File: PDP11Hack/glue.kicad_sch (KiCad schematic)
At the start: 5 parts, among them U21 74HCT139, U22 74AHCT273, U23 74LS27, U24 74HCT04, U25 74LS153

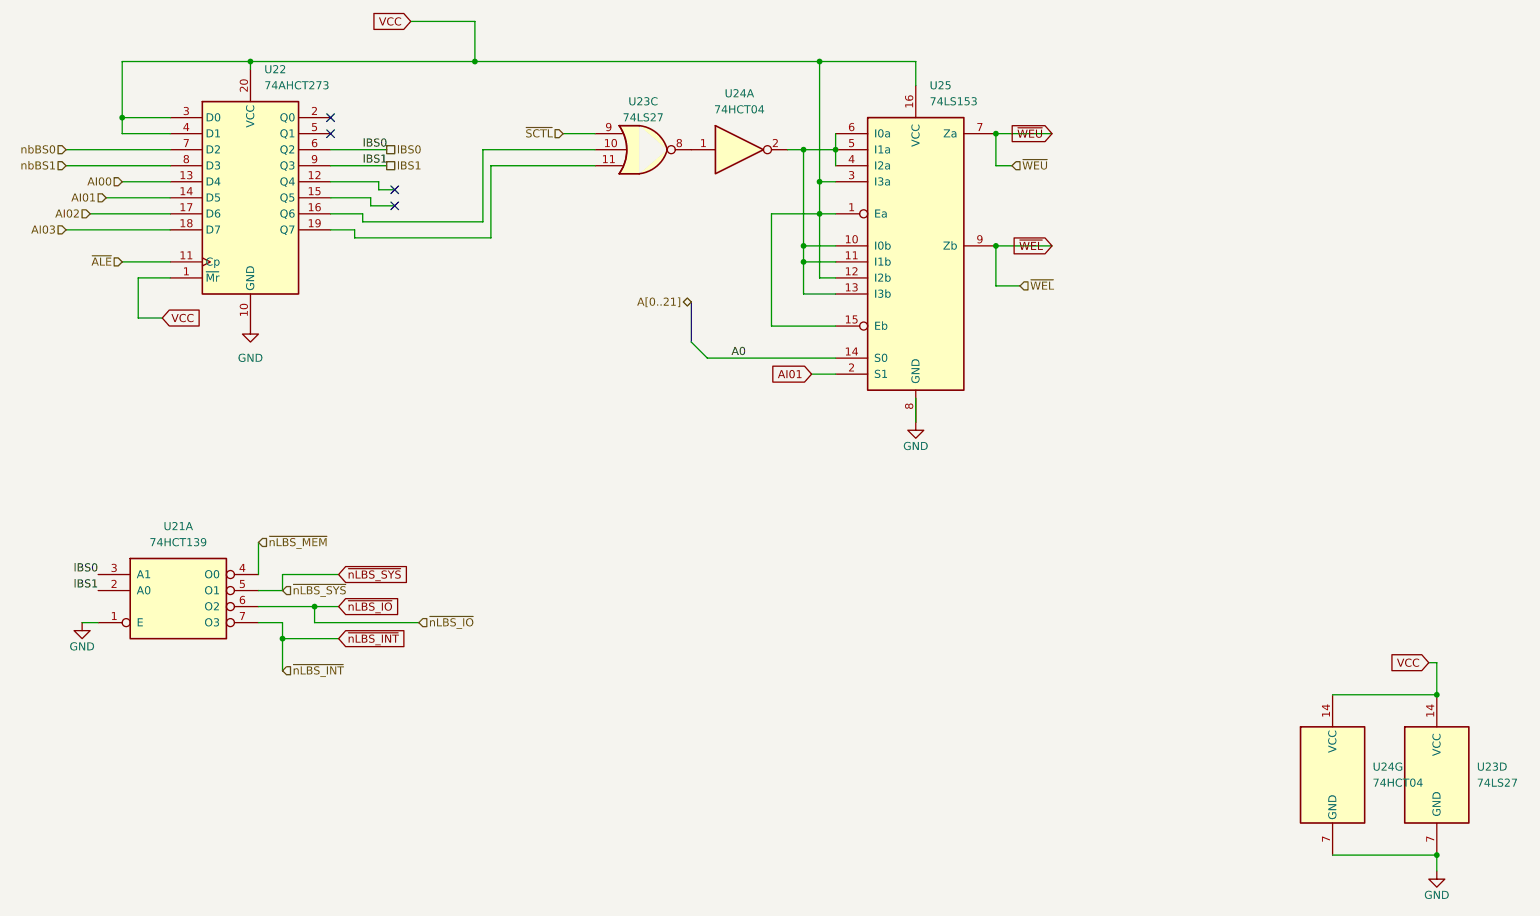
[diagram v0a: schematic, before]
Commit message: Corrections thanks to Peter Schranz on VCFED
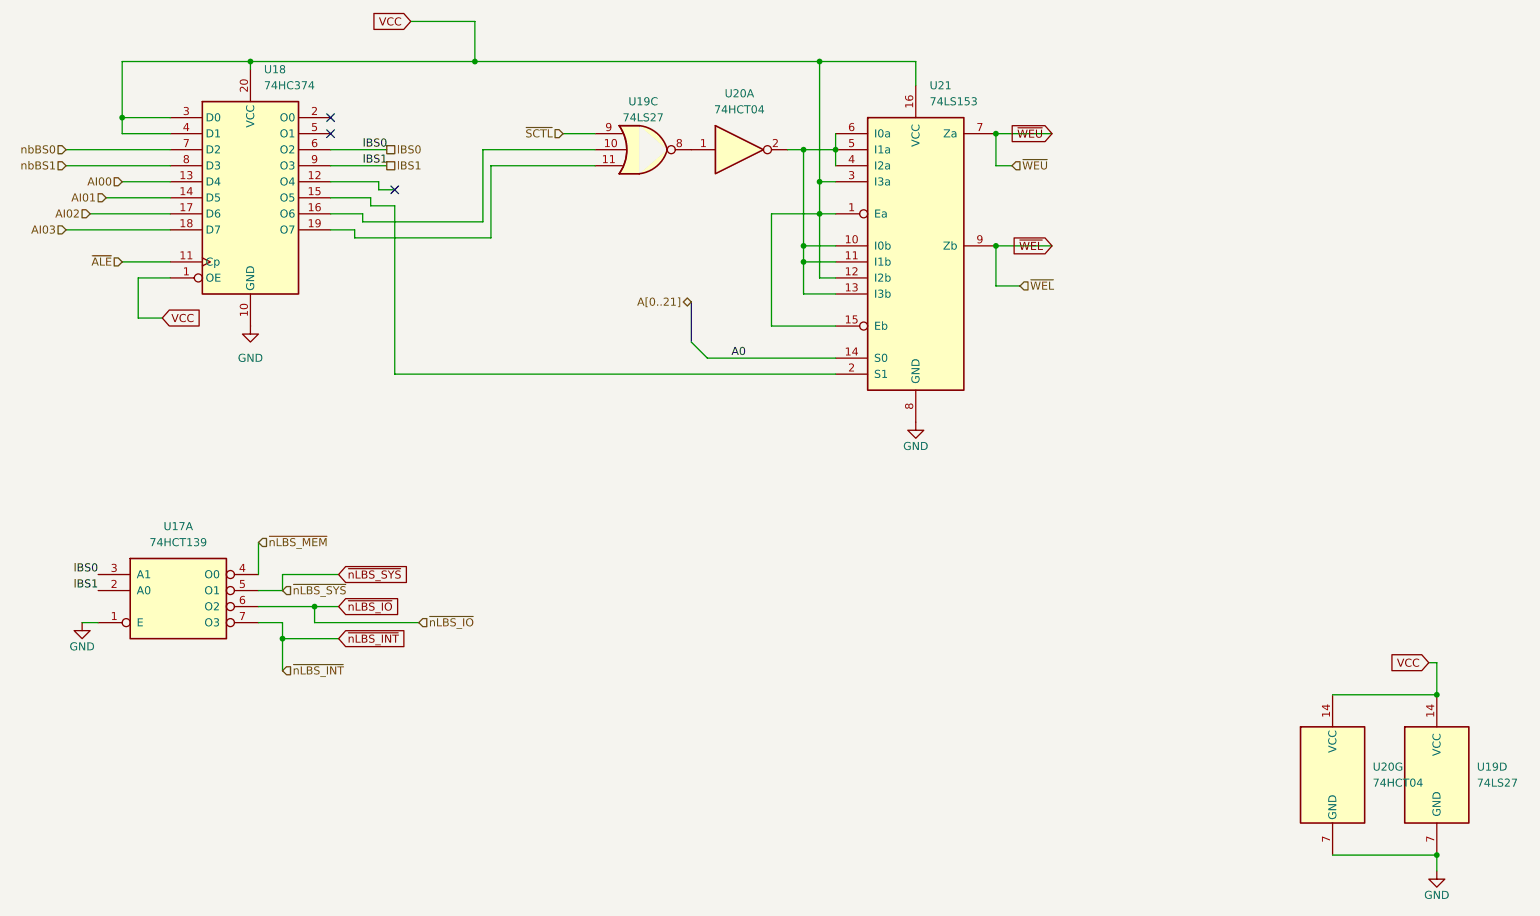
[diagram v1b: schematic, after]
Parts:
- removed U22: 74AHCT273, symbol 74xx:74AHCT273
- added U18: 74HC374, symbol 74xx:74HC374
- renumbered U21 to U17, U23 to U19, U24 to U20, U25 to U21
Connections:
- net AI00: now also U18.13 (D4)
- net AI01: now also U18.14 (D5); no longer U21.2 (S1)
- net AI02: now also U18.17 (D6)
- net AI03: now also U18.18 (D7)
- net GND: now also U18.10 (GND)
- net VCC: now also U18.1 (OE), U18.20 (VCC), U18.3 (D0), U18.4 (D1)
- net lBS0: now also U18.6 (O2)
- net lBS1: now also U18.9 (O3)
- net nbBS0: now also U18.7 (D2)
- net nbBS1: now also U18.8 (D3)
- net ~{ALE}: now also U18.11 (Cp)
- net at U19.10: now also U18.16 (O6)
- net at U19.11: now also U18.19 (O7)
- new net: U18.15 (O5), U21.2 (S1)
- no-connect marks 4 -> 3
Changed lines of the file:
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@@
-	)
-	(no_connect
-		(at 100.33 53.34)
 	)
 	(no_connect
@@
 	(wire
 		(pts
+			(xy 100.33 53.34) (xy 100.33 80.01)
+		)
+		(stroke
+			(width 0)
+			(type default)
+		)
+	)
+	(wire
+		(pts
 			(xy 78.74 116.84) (xy 87.63 116.84)
 		)
@@
 	(wire
 		(pts
-			(xy 166.37 80.01) (xy 170.18 80.01)
-		)
-		(stroke
-			(width 0)
-			(type default)
-		)
-	)
-	(wire
-		(pts
 			(xy 82.55 111.76) (xy 91.44 111.76)
 		)
@@
 	(wire
 		(pts
+			(xy 100.33 80.01) (xy 170.18 80.01)
+		)
+		(stroke
+			(width 0)
+			(type default)
+		)
+	)
+	(wire
+		(pts
 			(xy 90.17 54.61) (xy 95.25 54.61)
 		)
@@
 		(pts
 			(xy 57.15 49.53) (xy 64.77 49.53)
-		)
-		(stroke
-			(width 0)
-			(type default)
-		)
-	)
-	(wire
-		(pts
-			(xy 182.88 83.82) (xy 182.88 87.63)
 		)
 		(stroke
@@
 			)
 			(justify left bottom)
-		)
-	)
-	(global_label "AI01"
-		(shape input)
-		(at 166.37 80.01 180)
-		(fields_autoplaced yes)
-		(effects
-			(font
-				(size 1.27 1.27)
-			)
-			(justify right)
-		)
-		(property "Intersheetrefs" "${INTERSHEET_REFS}"
-			(at 159.2724 80.01 0)
-			(effects
-				(font
-					(size 1.27 1.27)
-				)
-				(justify right)
-				(hide yes)
-			)
 		)
 	)
@@
 		(dnp no)
 		(fields_autoplaced yes)
-		(property "Reference" "U23"
+		(property "Reference" "U19"
 			(at 139.7 36.83 0)
 			(effects
@@
 			(project "Modular DCJ11"
 				(path "/264d9b66-53d1-4564-94e8-42c7c0bb6a66/227e0659-a0cd-47a6-aec8-ce37362b6db6"
-					(reference "U23")
+					(reference "U19")
 					(unit 3)
 				)
@@
 		(dnp no)
 		(fields_autoplaced yes)
-		(property "Reference" "U25"
+		(property "Reference" "U21"
 			(at 185.0741 34.29 0)
 			(effects
@@
 			(project "Modular DCJ11"
 				(path "/264d9b66-53d1-4564-94e8-42c7c0bb6a66/227e0659-a0cd-47a6-aec8-ce37362b6db6"
-					(reference "U25")
+					(reference "U21")
 					(unit 1)
 				)
@@
 		(dnp no)
 		(fields_autoplaced yes)
-		(property "Reference" "U24"
+		(property "Reference" "U20"
 			(at 154.94 35.56 0)
 			(effects
@@
 			(project "Modular DCJ11"
 				(path "/264d9b66-53d1-4564-94e8-42c7c0bb6a66/227e0659-a0cd-47a6-aec8-ce37362b6db6"
-					(reference "U24")
+					(reference "U20")
 					(unit 1)
 				)
@@
 		(on_board yes)
 		(dnp no)
-		(property "Reference" "#PWR063"
+		(property "Reference" "#PWR061"
 			(at 182.88 93.98 0)
 			(effects
@@
 			(project "Modular DCJ11"
 				(path "/264d9b66-53d1-4564-94e8-42c7c0bb6a66/227e0659-a0cd-47a6-aec8-ce37362b6db6"
-					(reference "#PWR063")
+					(reference "#PWR061")
 					(unit 1)
 				)
@@
 		(on_board yes)
 		(dnp no)
-		(property "Reference" "#PWR061"
+		(property "Reference" "#PWR059"
 			(at 50.8 125.73 0)
 			(effects
@@
 			(project "Modular DCJ11"
 				(path "/264d9b66-53d1-4564-94e8-42c7c0bb6a66/227e0659-a0cd-47a6-aec8-ce37362b6db6"
-					(reference "#PWR061")
+					(reference "#PWR059")
 					(unit 1)
 				)
@@
 		(dnp no)
 		(fields_autoplaced yes)
-		(property "Reference" "U24"
+		(property "Reference" "U20"
 			(at 255.27 142.2399 0)
 			(effects
@@
 			(project "Modular DCJ11"
 				(path "/264d9b66-53d1-4564-94e8-42c7c0bb6a66/227e0659-a0cd-47a6-aec8-ce37362b6db6"
-					(reference "U24")
+					(reference "U20")
 					(unit 7)
+				)
+			)
+		)
+	)
+	(symbol
+		(lib_id "74xx:74HC374")
+		(at 77.47 52.07 0)
+		(unit 1)
+		(exclude_from_sim no)
+		(in_bom yes)
+		(on_board yes)
+		(dnp no)
+		(fields_autoplaced yes)
+		(property "Reference" "U18"
+			(at 79.6133 31.75 0)
+			(effects
+				(font
+					(size 1.27 1.27)
+				)
+				(justify left)
+			)
+		)
+		(property "Value" "74HC374"
+			(at 79.6133 34.29 0)
+			(effects
+				(font
+					(size 1.27 1.27)
+				)
+				(justify left)
+			)
+		)
+		(property "Footprint" ""
+			(at 77.47 52.07 0)
+			(effects
+				(font
+					(size 1.27 1.27)
+				)
+				(hide yes)
+			)
+		)
+		(property "Datasheet" "https://www.ti.com/lit/ds/symlink/cd74hct374.pdf"
+			(at 77.47 52.07 0)
+			(effects
+				(font
+					(size 1.27 1.27)
+				)
+				(hide yes)
+			)
+		)
+		(property "Description" "8-bit Register, 3-state outputs"
+			(at 77.47 52.07 0)
+			(effects
+				(font
+					(size 1.27 1.27)
+				)
+				(hide yes)
+			)
+		)
+		(pin "10"
+		)
+		(pin "14"
+		)
+		(pin "17"
+		)
+		(pin "11"
+		)
+		(pin "16"
+		)
+		(pin "15"
+		)
+		(pin "1"
+		)
+		(pin "7"
+		)
+		(pin "4"
+		)
+		(pin "18"
+		)
+		(pin "3"
+		)
+		(pin "5"
+		)
+		(pin "20"
+		)
+		(pin "6"
+		)
+		(pin "2"
+		)
+		(pin "19"
+		)
+		(pin "12"
+		)
+		(pin "9"
+		)
+		(pin "8"
+		)
+		(pin "13"
+		)
+		(instances
+			(project ""
+				(path "/264d9b66-53d1-4564-94e8-42c7c0bb6a66/227e0659-a0cd-47a6-aec8-ce37362b6db6"
+					(reference "U18")
+					(unit 1)
 				)
 			)
@@
 		(on_board yes)
 		(dnp no)
-		(property "Reference" "#PWR074"
+		(property "Reference" "#PWR062"
 			(at 265.43 165.1 0)
 			(effects
@@
 			(project "Modular DCJ11"
 				(path "/264d9b66-53d1-4564-94e8-42c7c0bb6a66/227e0659-a0cd-47a6-aec8-ce37362b6db6"
-					(reference "#PWR074")
+					(reference "#PWR062")
 					(unit 1)
 				)
@@
 		(dnp no)
 		(fields_autoplaced yes)
-		(property "Reference" "U23"
+		(property "Reference" "U19"
 			(at 271.78 142.2399 0)
 			(effects
@@
 			(project "Modular DCJ11"
 				(path "/264d9b66-53d1-4564-94e8-42c7c0bb6a66/227e0659-a0cd-47a6-aec8-ce37362b6db6"
-					(reference "U23")
+					(reference "U19")
 					(unit 4)
 				)
@@
 		(dnp no)
 		(fields_autoplaced yes)
-		(property "Reference" "U21"
+		(property "Reference" "U17"
 			(at 66.04 104.14 0)
 			(effects
@@
 			(project "Modular DCJ11"
 				(path "/264d9b66-53d1-4564-94e8-42c7c0bb6a66/227e0659-a0cd-47a6-aec8-ce37362b6db6"
-					(reference "U21")
+					(reference "U17")
 					(unit 1)
 				)
@@
 		(dnp no)
 		(fields_autoplaced yes)
-		(property "Reference" "#PWR062"
+		(property "Reference" "#PWR060"
 			(at 77.47 78.74 0)
 			(effects
@@
 			(project "Modular DCJ11"
 				(path "/264d9b66-53d1-4564-94e8-42c7c0bb6a66/227e0659-a0cd-47a6-aec8-ce37362b6db6"
-					(reference "#PWR062")
+					(reference "#PWR060")
 					(unit 1)
 				)
-			)
-		)
-	)
-	(symbol
-		(lib_id "74xx:74AHCT273")
-		(at 77.47 52.07 0)
-		(unit 1)
-		(exclude_from_sim no)
-		(in_bom yes)
-		(on_board yes)
-		(dnp no)
-		(fields_autoplaced yes)
-		(property "Reference" "U22"
-			(at 79.6641 31.75 0)
-			(effects
-				(font
-					(size 1.27 1.27)
-				)
-				(justify left)
-			)
-		)
-		(property "Value" "74AHCT273"
-			(at 79.6641 34.29 0)
-			(effects
-				(font
-					(size 1.27 1.27)
-				)
-				(justify left)
-			)
-		)
-		(property "Footprint" ""
-			(at 77.47 52.07 0)
-			(effects
-				(font
-					(size 1.27 1.27)
-				)
-				(hide yes)
-			)
-		)
-		(property "Datasheet" "https://assets.nexperia.com/documents/data-sheet/74AHC_AHCT273.pdf"
-			(at 77.47 52.07 0)
-			(effects
-				(font
-					(size 1.27 1.27)
-				)
-				(hide yes)
-			)
-		)
-		(property "Description" ""
-			(at 77.47 52.07 0)
-			(effects
-				(font
-					(size 1.27 1.27)
-				)
-			)
-		)
-		(pin "1"
-		)
-		(pin "10"
-		)
-		(pin "11"
-		)
-		(pin "12"
-		)
-		(pin "13"
-		)
-		(pin "14"
-		)
-		(pin "15"
-		)
-		(pin "16"
-		)
-		(pin "17"
-		)
-		(pin "18"
-		)
-		(pin "19"
-		)
-		(pin "2"
-		)
-		(pin "20"
-		)
-		(pin "3"
-		)
-		(pin "4"
-		)
-		(pin "5"
-		)
-		(pin "6"
-		)
-		(pin "7"
-		)
-		(pin "8"
-		)
-		(pin "9"
-		)
-		(instances
-			(project "Modular DCJ11"
-				(path "/264d9b66-53d1-4564-94e8-42c7c0bb6a66/227e0659-a0cd-47a6-aec8-ce37362b6db6"
-					(reference "U22")
-					(unit 1)
-				)

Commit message: Last update, PCB creation ready
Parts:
- removed U20: 74HCT04, symbol 74xx:74HCT04
- added unit 2 of U19
- added unit 1 of U19
- added U2: 74HCT04, Package_DIP:DIP-14_W7.62mm, symbol 74xx:74HCT04
- U17, U21: footprint (none) -> Package_DIP:DIP-16_W7.62mm
- U18: footprint (none) -> Package_DIP:DIP-20_W7.62mm
- U19: footprint (none) -> Package_DIP:DIP-14_W7.62mm
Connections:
- net GND: now also U19.1, U19.13, U19.2, U19.3, U19.4, U19.5
- net at U19.8: now also U2.5
- net at U21.10 (I0b), U21.11 (I1b), U21.13 (I3b)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: now also U2.6
- no-connect marks 3 -> 5
